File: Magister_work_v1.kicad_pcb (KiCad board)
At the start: 4 copper layers, 65 x 81 mm, 152 parts, among them J1 USB_B_Mini, J15 Conn_01x02_Pin, J17 Conn_01x04_Pin, J3 Conn_01x03_Pin, J6 Conn_01x04_Pin, J7 Conn_01x02_Pin, J8 Conn_01x06_Pin, J9 Conn_01x02_Pin, Q1 AO3400A, Q2 AO3400A, Q3 PDTC143ET, Q4 PDTC143ET, Q5 PDTC143ET, Q6 PDTC143ET, Q7 PDTC143ET, Q8 PDTC143ET, SW1 SW_Push, SW10 SW_Push, SW11 SW_Push, SW12 SW_Push, SW2 SW_Push, SW3 SW_Push, SW4 SW_Push, SW5 SW_Push, SW6 SW_Push, SW7 SW_Push, SW8 SW_Push, SW9 SW_Push, U10 SRV05-4, U3 Ai-Thinker-Ra-01, U5 AMS1117-3.3, U7 STM32F407VETx, U8 AT24C256, U9 Ai-Thinker-Ra-01SH, Y1 X322525MQB4SI, Y2 SMD03215C2

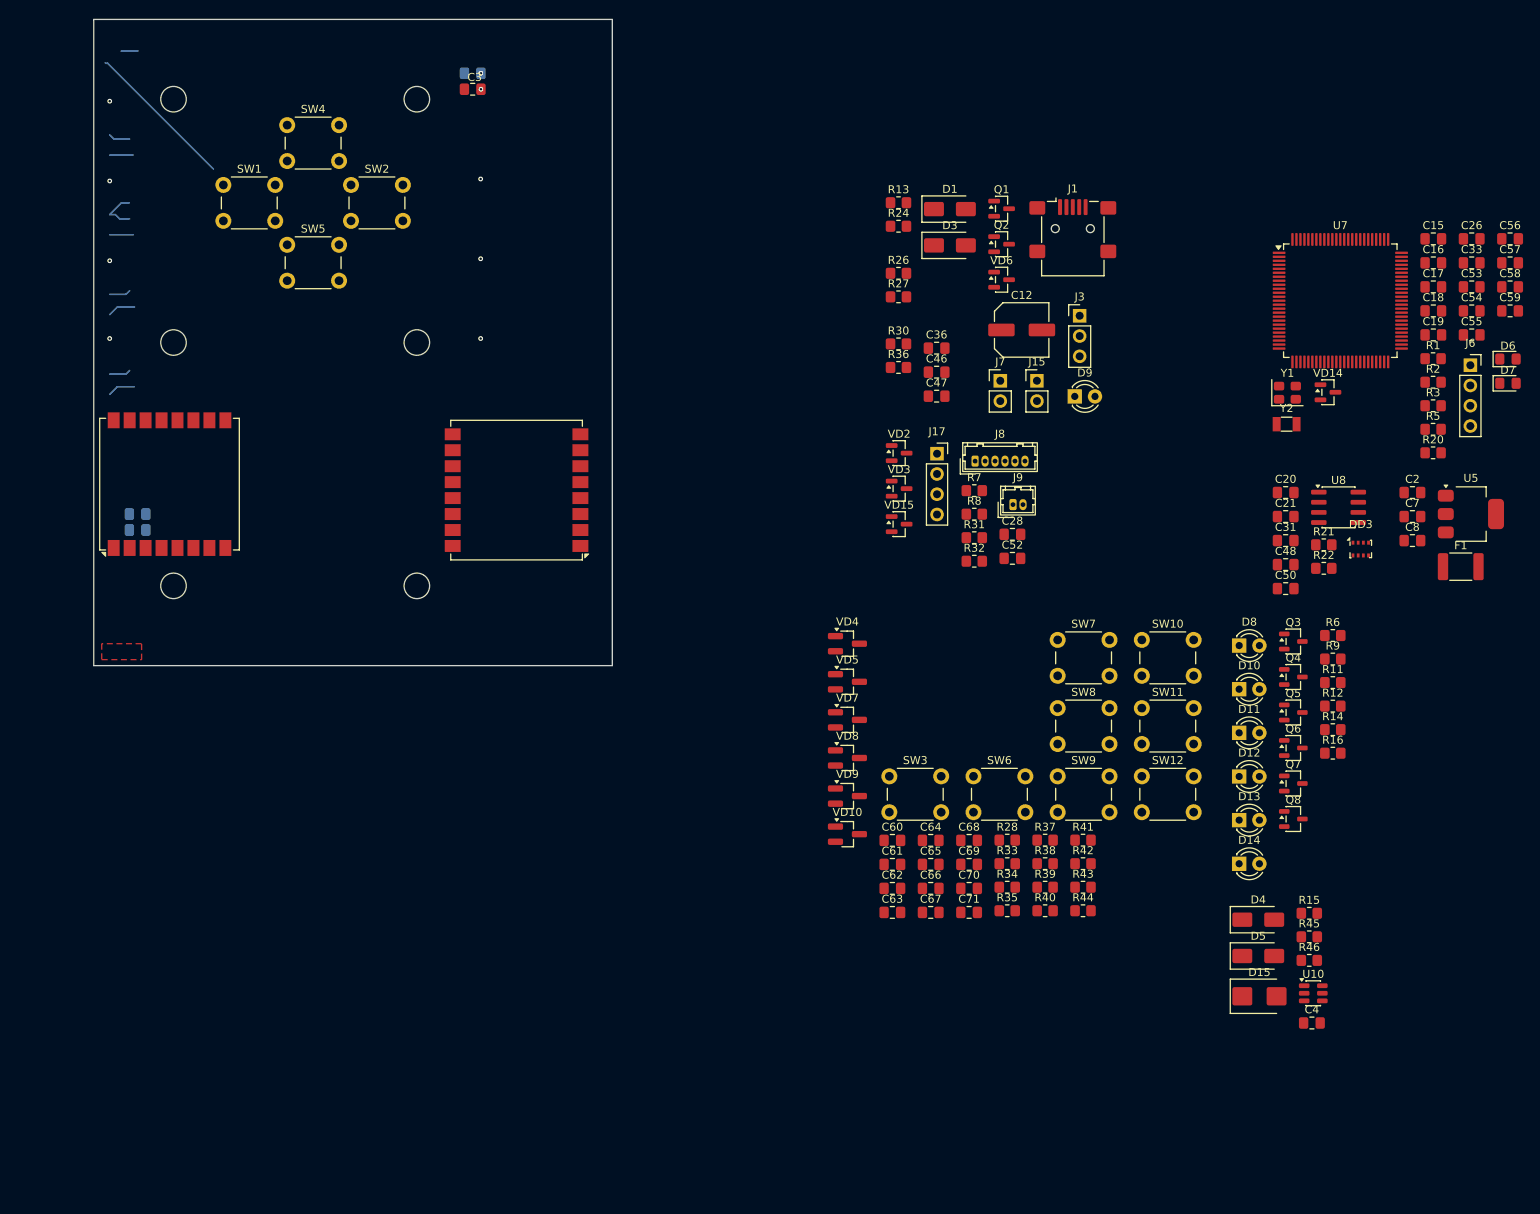
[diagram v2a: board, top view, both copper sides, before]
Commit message: feat: добавлены связи цифровых линий с МК
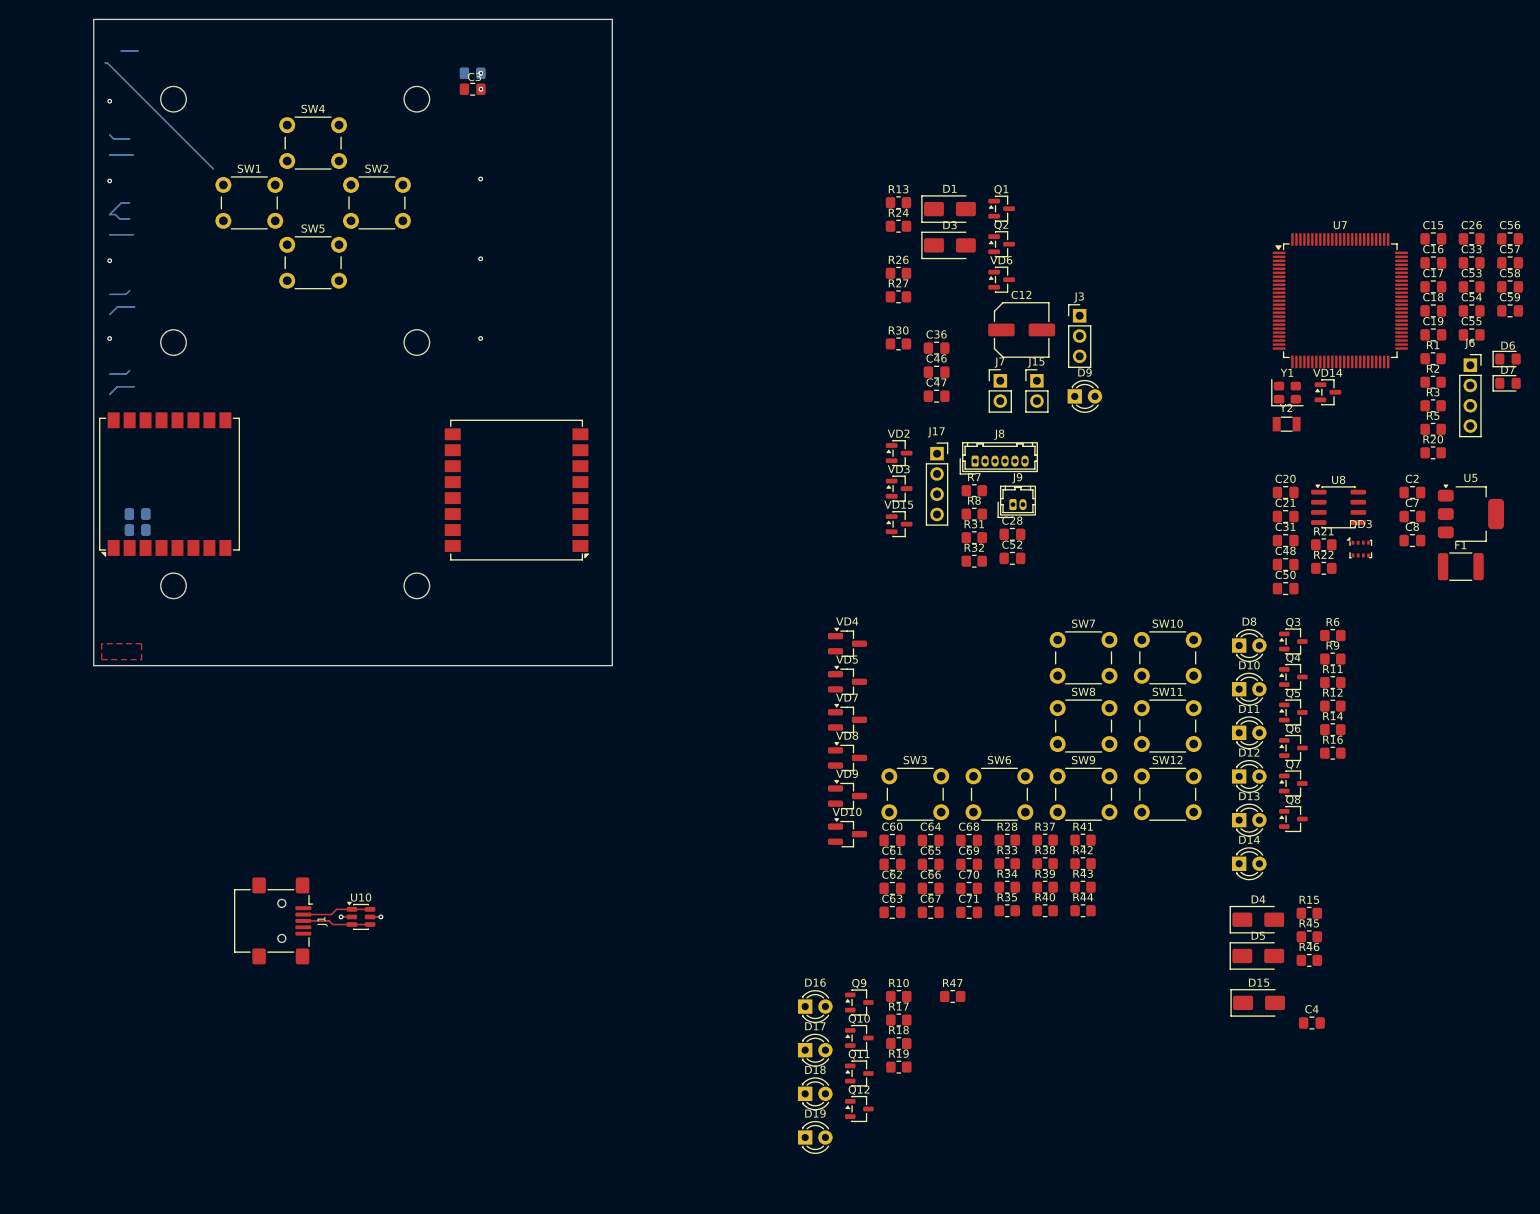
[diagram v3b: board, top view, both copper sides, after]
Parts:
- removed R36: 220, Resistor_SMD:R_0805_2012Metric_Pad1.20x1.40mm_HandSolder
- added D16: LED, LED_THT:LED_D3.0mm, F.Cu at (119.2, 153.7)
- added D17: LED, LED_THT:LED_D3.0mm, F.Cu at (119.2, 159.2)
- added D18: LED, LED_THT:LED_D3.0mm, F.Cu at (119.2, 164.7)
- added D19: LED, LED_THT:LED_D3.0mm, F.Cu at (119.2, 170.1)
- added Q10: PDTC143ET, Package_TO_SOT_SMD:SOT-23-3, F.Cu at (126.0, 157.7)
- added Q11: PDTC143ET, Package_TO_SOT_SMD:SOT-23-3, F.Cu at (126.0, 162.1)
- added Q12: PDTC143ET, Package_TO_SOT_SMD:SOT-23-3, F.Cu at (126.0, 166.6)
- added Q9: PDTC143ET, Package_TO_SOT_SMD:SOT-23-3, F.Cu at (126.0, 153.2)
- added R10: 220, Resistor_SMD:R_0805_2012Metric_Pad1.20x1.40mm_HandSolder, F.Cu at (130.9, 152.5)
- added R17: 220, Resistor_SMD:R_0805_2012Metric_Pad1.20x1.40mm_HandSolder, F.Cu at (130.9, 155.4)
- added R18: 220, Resistor_SMD:R_0805_2012Metric_Pad1.20x1.40mm_HandSolder, F.Cu at (130.9, 158.4)
- added R19: 220, Resistor_SMD:R_0805_2012Metric_Pad1.20x1.40mm_HandSolder, F.Cu at (130.9, 161.3)
- added R47: 100, Resistor_SMD:R_0805_2012Metric_Pad1.20x1.40mm_HandSolder, F.Cu at (137.7, 152.5)
- D15: value SMBJ5.0CA -> SMAJ5.0CA; footprint Diode_SMD:D_SMB -> Diode_SMD:D_SMA
- R45, R46: value 220 -> 100
- moved J1 131.8 mm to (53.6, 143.0), turned to -90 degrees
- moved U10 119.7 mm to (63.5, 142.5)
- moved D15 0.83 mm to (176.1, 153.3)
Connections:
- C62 pad 2: Net-(C62-Pad2) -> DI5
- C63 pad 2: Net-(C63-Pad2) -> DI6
- C64 pad 2: Net-(C64-Pad2) -> DI9
- C65 pad 2: Net-(C65-Pad2) -> DI10
- C68 pad 2: Net-(C68-Pad2) -> DI7
- C69 pad 2: Net-(C69-Pad2) -> DI8
- C70 pad 2: Net-(C70-Pad2) -> DI11
- C71 pad 2: Net-(C71-Pad2) -> DI12
- D9 pad 1: Net-(D9-K) -> GND
- D9 pad 2: +5V -> Net-(D9-A)
- DD3 pad 3: LSM_SDI -> SDI_BMP280
- DD3 pad 4: LSM_SCLK -> SCK_BMP280
- DD3 pad 5: LSM_SDO -> SDO_BMP280
- J1 pad 2: unconnected-(J1-D--Pad2) -> D-
- J1 pad 3: unconnected-(J1-D+-Pad3) -> D+
- J17 pad 2: DEBUG_RX2 -> DEBUG_RX1
- J17 pad 3: DEBUG_TX2 -> DEBUG_TX1
- J3 pad 3: PWM2 -> PWM1
- Q3 pad 1: /LEDs/DO1 -> DO1
- Q4 pad 1: /LEDs/DO2 -> DO2
- Q5 pad 1: /LEDs/DO3 -> DO3
- Q6 pad 1: /LEDs/DO4 -> DO4
- Q7 pad 1: /LEDs/DO5 -> DO5
- Q8 pad 1: /LEDs/DO6 -> DO6
- R37 pad 1: Net-(C62-Pad2) -> DI5
- R38 pad 1: Net-(C63-Pad2) -> DI6
- R39 pad 1: Net-(C68-Pad2) -> DI7
- R40 pad 1: Net-(C69-Pad2) -> DI8
- R41 pad 1: Net-(C64-Pad2) -> DI9
- R42 pad 1: Net-(C65-Pad2) -> DI10
- R43 pad 1: Net-(C70-Pad2) -> DI11
- R44 pad 1: Net-(C71-Pad2) -> DI12
- U10 pad 1: /PWR_Sheet/D+ -> D-
- U10 pad 3: /PWR_Sheet/D- -> D+
- U10 pad 4: unconnected-(U10-IO3-Pad4) -> D+
- U10 pad 6: unconnected-(U10-IO4-Pad6) -> D-
- U7 pad 18: BAT_CTRL -> unconnected-(U7-PC3-Pad18)
- U7 pad 23: PWM5 -> unconnected-(U7-PA0-Pad23)
- U7 pad 24: PWM6 -> unconnected-(U7-PA1-Pad24)
- U7 pad 41: unconnected-(U7-PE10-Pad41) -> DO1
- U7 pad 42: PWM2 -> DO2
- U7 pad 43: unconnected-(U7-PE12-Pad43) -> DO3
- U7 pad 44: PWM3 -> DO4
- U7 pad 45: PWM4 -> DO5
- U7 pad 46: unconnected-(U7-PE15-Pad46) -> DO6
- U7 pad 47: PWM7 -> BN_880_SCL
- U7 pad 48: PWM8 -> BN_880_SDA
- U7 pad 51: BMI270_CS -> unconnected-(U7-PB12-Pad51)
- U7 pad 52: BMI270_SCLK -> SCK_RaSH
- U7 pad 53: BMI270_SDO -> MISO_RaSH
- U7 pad 54: BMI270_SDI -> MOSI_RaSH
- U7 pad 55: DEBUG_TX2 -> DI5
- U7 pad 56: DEBUG_RX2 -> DI6
- U7 pad 57: BMI270_INT1 -> DI7
- U7 pad 58: BMI270_INT2 -> DI8
- U7 pad 59: MPU_CS -> DI9
- U7 pad 60: MPU_INT -> DI10
- U7 pad 61: unconnected-(U7-PD14-Pad61) -> DI11
- U7 pad 62: unconnected-(U7-PD15-Pad62) -> DI12
- U7 pad 66: BN_880_SDA -> unconnected-(U7-PC9-Pad66)
- U7 pad 67: BN_880_SCL -> unconnected-(U7-PA8-Pad67)
- U7 pad 70: unconnected-(U7-PA11-Pad70) -> D-
- U7 pad 71: unconnected-(U7-PA12-Pad71) -> D+
- U7 pad 78: LSM_SCLK -> UART4_TX
- U7 pad 79: LSM_SDO -> UART4_RX
- U7 pad 80: LSM_SDI -> unconnected-(U7-PC12-Pad80)
- U7 pad 81: LSM_CS -> DO7
- U7 pad 82: LSM_INT1 -> DO8
- U7 pad 83: LSM_INT2 -> DO9
- U7 pad 84: unconnected-(U7-PD3-Pad84) -> DO10
- U7 pad 85: unconnected-(U7-PD4-Pad85) -> DI1
- U7 pad 86: unconnected-(U7-PD5-Pad86) -> DI2
- U7 pad 87: unconnected-(U7-PD6-Pad87) -> DI3
- U7 pad 88: unconnected-(U7-PD7-Pad88) -> DI4
- U7 pad 89: unconnected-(U7-PB3-Pad89) -> SCK_BMP280
- U7 pad 90: unconnected-(U7-PB4-Pad90) -> SDO_BMP280
- U7 pad 91: unconnected-(U7-PB5-Pad91) -> SDI_BMP280
- U9 pad 12: SCK_LoRa -> SCK_RaSH
- U9 pad 13: MISO_LoRa -> MISO_RaSH
- U9 pad 14: MOSI_LoRa -> MOSI_RaSH
- VD15 pad 1: DEBUG_RX2 -> DEBUG_RX1
- VD15 pad 2: DEBUG_TX2 -> DEBUG_TX1
- VD6 pad 1: PWM2 -> PWM1
- VD6 pad 2: PWM2 -> PWM1
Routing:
- net (no net): track 13.9 -> 26.8 mm
- net D-: track 0.00 -> 8.63 mm
- net D+: track 0.00 -> 8.55 mm
- net PWM7: track 3.52 -> 0.00 mm
- net PWM8: track 3.46 -> 0.00 mm
- net PWM6: track 2.95 -> 0.00 mm
- net PWM5: track 2.95 -> 0.00 mm
- net GND: track 0.00 -> 1.36 mm, vias 9 -> 10
- net +5V: track 0.00 -> 1.36 mm, vias 0 -> 1

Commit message: feat: добавлен дополнительный разъём для питания
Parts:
- added C5: 0.1u, Capacitor_SMD:C_0805_2012Metric_Pad1.18x1.45mm_HandSolder, F.Cu at (57.0, 166.1)
- added C6: 0.1u, Capacitor_SMD:C_0805_2012Metric_Pad1.18x1.45mm_HandSolder, F.Cu at (57.0, 169.1)
- added C9: 0.1u, Capacitor_SMD:C_0805_2012Metric_Pad1.18x1.45mm_HandSolder, F.Cu at (57.0, 172.1)
- added D2: SS32, Diode_SMD:D_SMA, F.Cu at (50.6, 166.8)
- added D20: SMAJ5.0CA, Diode_SMD:D_SMA, F.Cu at (50.6, 171.4)
- added J2: Conn_01x03_Pin, Connector_JST:JST_NV_B03P-NV_1x03_P5.00mm_Vertical, F.Cu at (94.0, 35.5)
- moved C1 133.8 mm to (81.5, 170.5)
- moved C3 133.8 mm to (81.5, 172.5)
- moved J1 109.6 mm to (79.7, 36.5), turned to 180 degrees
- moved U5 107.6 mm to (101.0, 56.5)
- moved U10 97.5 mm to (80.2, 46.5), turned to -90 degrees
- moved SW1 95.8 mm to (21.2, 143.2)
- moved SW2 95.8 mm to (37.2, 143.2)
- moved SW4 95.8 mm to (29.2, 135.8)
- moved SW5 95.8 mm to (29.2, 150.8)
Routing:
- net (no net): track 26.8 -> 0.00 mm
- net POWER_DO2: track 19.1 -> 0.00 mm
- net Net-(Q2-G): track 2.15 -> 0.00 mm
- net GND: vias 10 -> 3
- removed copper zone on F.Cu, net GND
- removed copper zone on In1.Cu, net GND
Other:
- board size 65 x 81 mm -> 80 x 81 mm

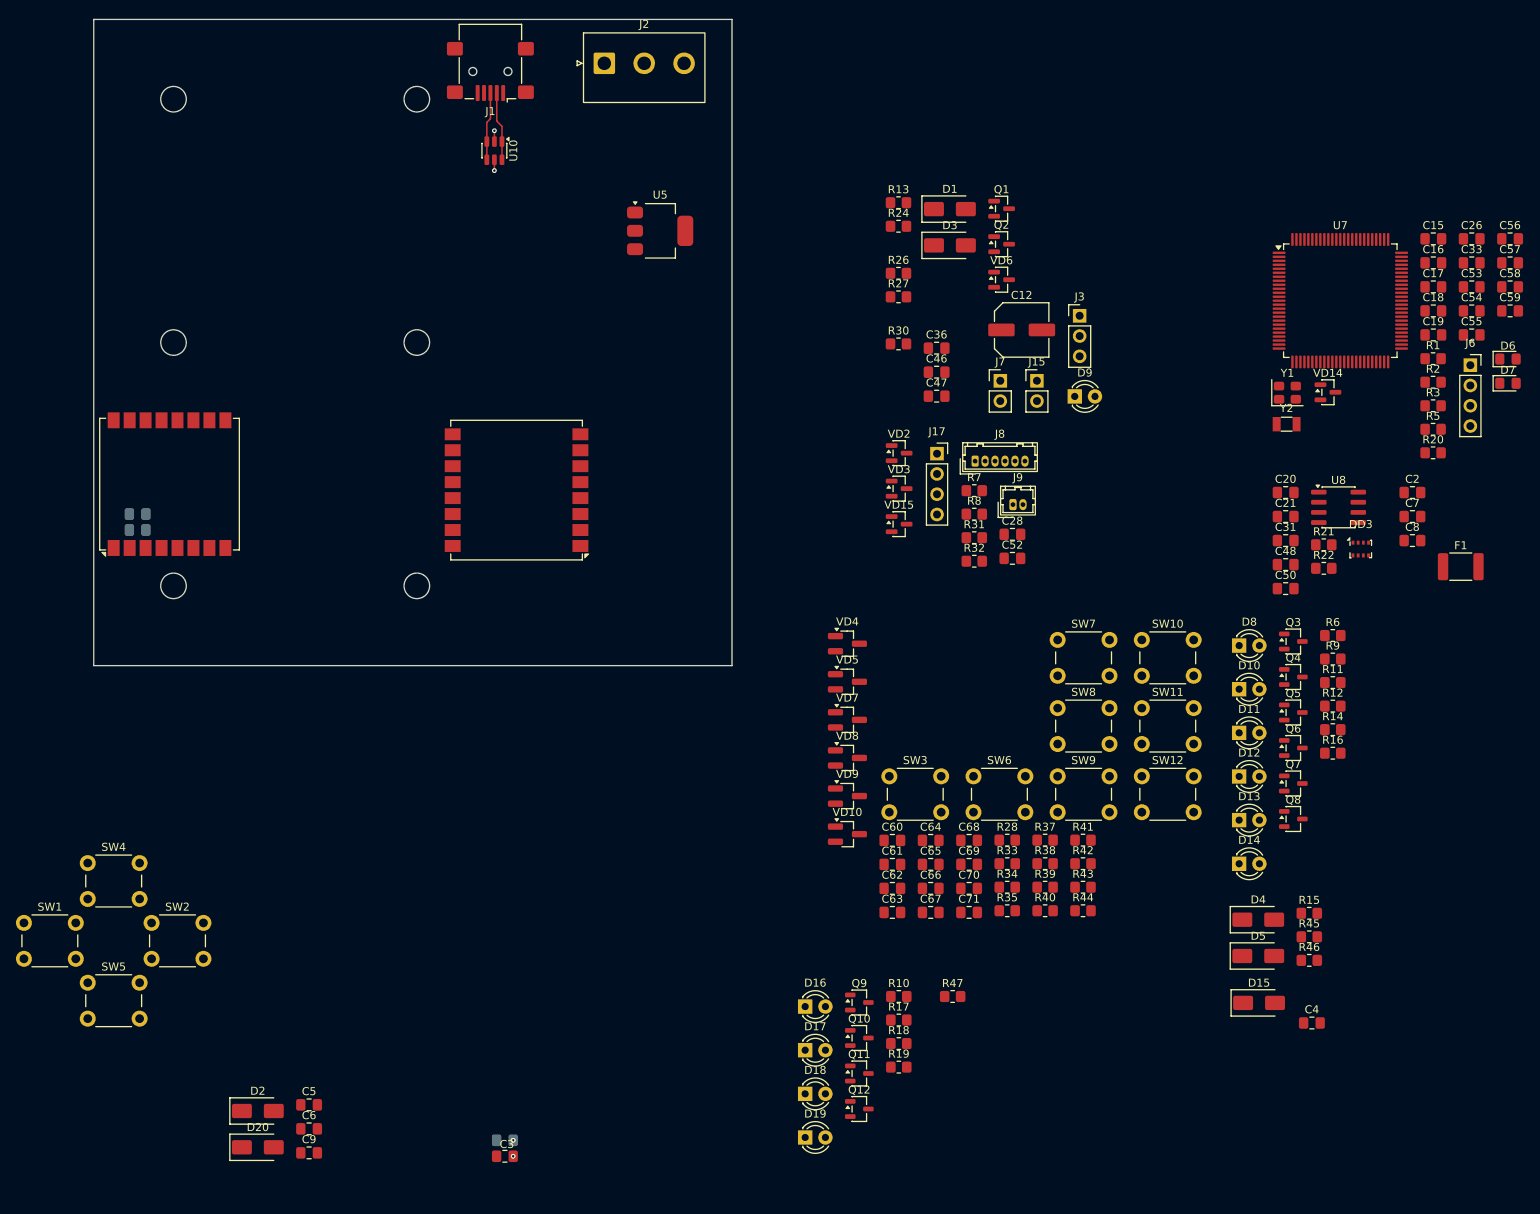
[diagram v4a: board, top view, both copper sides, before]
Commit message: feat: укомплектовал основные узлы модуля на печатной платы для первичной компановки
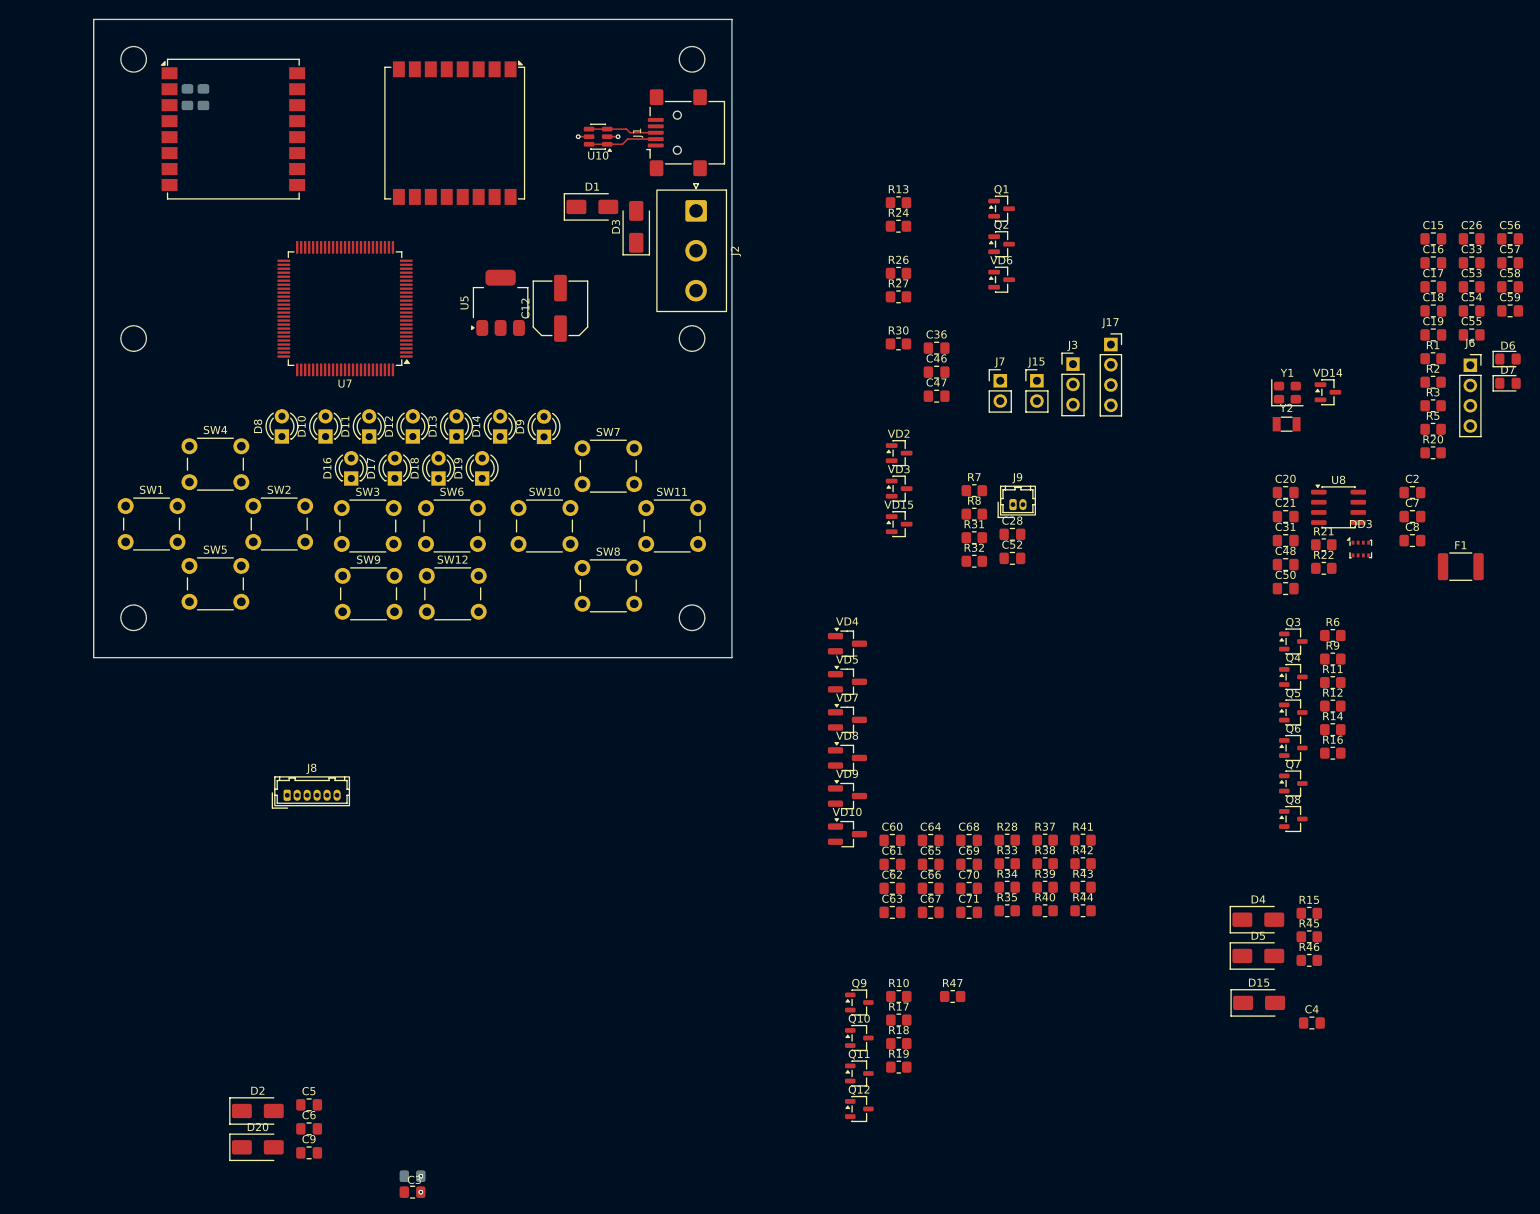
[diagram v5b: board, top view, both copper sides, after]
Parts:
- moved U7 124.8 mm to (61.5, 66.2), turned to 180 degrees
- moved D8 122.8 mm to (53.6, 82.3), turned to 90 degrees
- moved D10 118.8 mm to (59.1, 82.3), turned to 90 degrees
- moved D11 115.2 mm to (64.5, 82.3), turned to 90 degrees
- moved D12 112.0 mm to (70.0, 82.3), turned to 90 degrees
- moved D13 109.3 mm to (75.5, 82.3), turned to 90 degrees
- moved D14 107.0 mm to (80.9, 82.3), turned to 90 degrees
- moved J8 95.9 mm to (54.2, 127.2)
- moved SW12 93.1 mm to (71.8, 99.8)
- moved SW9 93.1 mm to (61.2, 99.8)
- moved D19 92.0 mm to (78.7, 87.5), turned to 90 degrees
- moved D18 89.8 mm to (73.2, 87.5), turned to 90 degrees
- moved D17 88.2 mm to (67.8, 87.5), turned to 90 degrees
- moved D16 87.3 mm to (62.3, 87.5), turned to 90 degrees
- moved SW10 79.9 mm to (83.2, 91.2)
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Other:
- board size 80 x 81 mm -> 80 x 80 mm
